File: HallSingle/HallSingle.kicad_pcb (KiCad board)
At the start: 2 copper layers, 12 x 26 mm, 10 parts, among them J1 Conn_01x03, U1 SS49E, U2 TS331ILT

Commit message: Added Voron Logo and filled missing resistor value
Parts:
- added G***: LOGO, HallEffect:VoronLogo_6pt5mm_silkScreen, B.Cu at (144.0, 61.0)
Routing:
- net Signal: track 21.4 -> 24.4 mm
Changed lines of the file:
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@@
     (thickness 1.6)
     (drawings 9)
-    (tracks 29)
+    (tracks 28)
     (zones 0)
-    (modules 10)
+    (modules 11)
     (nets 8)
   )
@@
     (add_net GND)
   )
+  (module HallEffect:VoronLogo_6pt5mm_silkScreen (layer B.Cu)
+    (at 144 61 270)
+    (fp_text reference G*** (at 0 0 270) (layer B.SilkS) hide
+      (effects (font (size 1.524 1.524) (thickness 0.3)) (justify mirror))
+    )
+    (fp_text value LOGO (at 0.75 0 270) (layer B.SilkS) hide
+      (effects (font (size 1.524 1.524) (thickness 0.3)) (justify mirror))
+    )
+    (fp_poly (pts (xy 2.7686 1.64985) (xy 2.7686 -1.649849) (xy 1.379308 -2.450524) (xy 1.039339 -2.646185)
+      (xy 0.729012 -2.824267) (xy 0.458882 -2.978754) (xy 0.239505 -3.10363) (xy 0.081439 -3.192877)
+      (xy -0.004761 -3.240478) (xy -0.017692 -3.24677) (xy -0.061819 -3.221166) (xy -0.183209 -3.150713)
+      (xy -0.371255 -3.041566) (xy -0.615351 -2.899881) (xy -0.904891 -2.731815) (xy -1.229269 -2.543525)
+      (xy -1.397 -2.446162) (xy -2.622352 -1.734876) (xy -1.566334 -1.734876) (xy -1.527559 -1.754402)
+      (xy -1.409521 -1.769187) (xy -1.234533 -1.776891) (xy -1.159934 -1.777479) (xy -0.7366 -1.776959)
+      (xy -0.722179 -1.755076) (xy 0 -1.755076) (xy 0.04685 -1.765563) (xy 0.171616 -1.7735)
+      (xy 0.350623 -1.777596) (xy 0.4191 -1.777886) (xy 0.8382 -1.777772) (xy 1.3208 -1.034043)
+      (xy 1.485838 -0.779678) (xy 1.637963 -0.545166) (xy 1.765863 -0.347951) (xy 1.858223 -0.205476)
+      (xy 1.897288 -0.145156) (xy 1.991177 0) (xy 1.129093 0) (xy 0.564546 -0.866076)
+      (xy 0.394034 -1.128735) (xy 0.244186 -1.361619) (xy 0.123286 -1.551683) (xy 0.039618 -1.685882)
+      (xy 0.001465 -1.751172) (xy 0 -1.755076) (xy -0.722179 -1.755076) (xy 0.4064 -0.042603)
+      (xy 0.654036 0.333568) (xy 0.884037 0.683745) (xy 1.09042 0.998762) (xy 1.267202 1.269449)
+      (xy 1.408399 1.486639) (xy 1.508029 1.641163) (xy 1.560108 1.723852) (xy 1.566333 1.734877)
+      (xy 1.527558 1.754403) (xy 1.40952 1.769188) (xy 1.234532 1.776892) (xy 1.159933 1.77748)
+      (xy 0.7366 1.77696) (xy -0.4064 0.042604) (xy -0.654037 -0.333567) (xy -0.884038 -0.683744)
+      (xy -1.090421 -0.998761) (xy -1.267203 -1.269448) (xy -1.4084 -1.486638) (xy -1.50803 -1.641162)
+      (xy -1.560109 -1.723851) (xy -1.566334 -1.734876) (xy -2.622352 -1.734876) (xy -2.7686 -1.649983)
+      (xy -2.7686 0) (xy -1.991178 0) (xy -1.129094 0) (xy -0.564547 0.866077)
+      (xy -0.394035 1.128736) (xy -0.244187 1.36162) (xy -0.123287 1.551684) (xy -0.039619 1.685883)
+      (xy -0.001466 1.751173) (xy 0 1.755077) (xy -0.046851 1.765564) (xy -0.171617 1.773501)
+      (xy -0.350624 1.777597) (xy -0.4191 1.777887) (xy -0.8382 1.777773) (xy -1.3208 1.034044)
+      (xy -1.485839 0.779679) (xy -1.637964 0.545167) (xy -1.765864 0.347952) (xy -1.858224 0.205477)
+      (xy -1.897289 0.145157) (xy -1.991178 0) (xy -2.7686 0) (xy -2.7686 1.64985)
+      (xy 0 3.245448) (xy 2.7686 1.64985)) (layer B.SilkS) (width 0.01))
+  )
   (module HallEffect:SOT-23-5 (layer F.Cu)
     (at 147.5535 59.563)
@@
       (effects (font (size 1 1) (thickness 0.15)))
     )
-    (fp_text value R (at 0 1.65 90) (layer F.Fab)
+    (fp_text value R (at 3.3805 -0.0635 90) (layer F.Fab)
       (effects (font (size 1 1) (thickness 0.15)))
     )
@@
       (effects (font (size 1 1) (thickness 0.15)))
     )
-    (fp_text value 10K (at 0 1.65) (layer F.Fab)
+    (fp_text value 10K (at 0.3325 1.4605) (layer F.Fab)
       (effects (font (size 1 1) (thickness 0.15)))
     )
@@
     (attr smd)
     (fp_text reference D1 (at -0.063 -1.443 90) (layer F.SilkS)
-      (effects (font (size 0.5 0.5) (thickness 0.125)))
+      (effects (font (size 0.75 0.75) (thickness 0.125)))
     )
     (fp_text value LED (at 0 1.65 90) (layer F.Fab)
@@
       (effects (font (size 1 1) (thickness 0.15)))
     )
-    (fp_text value 1uF (at 0 1.65 90) (layer F.Fab)
+    (fp_text value 1uF (at 3.8885 0.254 90) (layer F.Fab)
       (effects (font (size 1 1) (thickness 0.15)))
     )
@@
       (effects (font (size 1 1) (thickness 0.15)))
     )
-    (fp_text value 0.1uF (at 0 1.65) (layer F.Fab)
+    (fp_text value 0.1uF (at 0 -2.0955) (layer F.Fab)
       (effects (font (size 1 1) (thickness 0.15)))
     )
@@
   (segment (start 148.463 62.738) (end 146.7485 62.738) (width 0.3048) (layer F.Cu) (net 2))
   (segment (start 146.558 64.9605) (end 146.558 62.9285) (width 0.3048) (layer F.Cu) (net 2))
+  (segment (start 148.6535 75.2665) (end 148 75.92) (width 0.3048) (layer B.Cu) (net 5))
+  (segment (start 148.6535 60.5155) (end 148.6535 75.2665) (width 0.3048) (layer B.Cu) (net 5))
   (segment (start 144.526 64.643) (end 148.6535 60.5155) (width 0.3048) (layer B.Cu) (net 5))
   (segment (start 141.6685 64.643) (end 144.526 64.643) (width 0.3048) (layer B.Cu) (net 5))
-  (segment (start 147.150001 67.267001) (end 144.526 64.643) (width 0.3048) (layer B.Cu) (net 5))
-  (segment (start 147.150001 75.070001) (end 147.150001 67.267001) (width 0.3048) (layer B.Cu) (net 5))
-  (segment (start 148 75.92) (end 147.150001 75.070001) (width 0.3048) (layer B.Cu) (net 5))
   (segment (start 146.451 58.6105) (end 146.4535 58.613) (width 0.3048) (layer F.Cu) (net 7))
   (segment (start 144.272 58.6105) (end 146.451 58.6105) (width 0.3048) (layer F.Cu) (net 7))

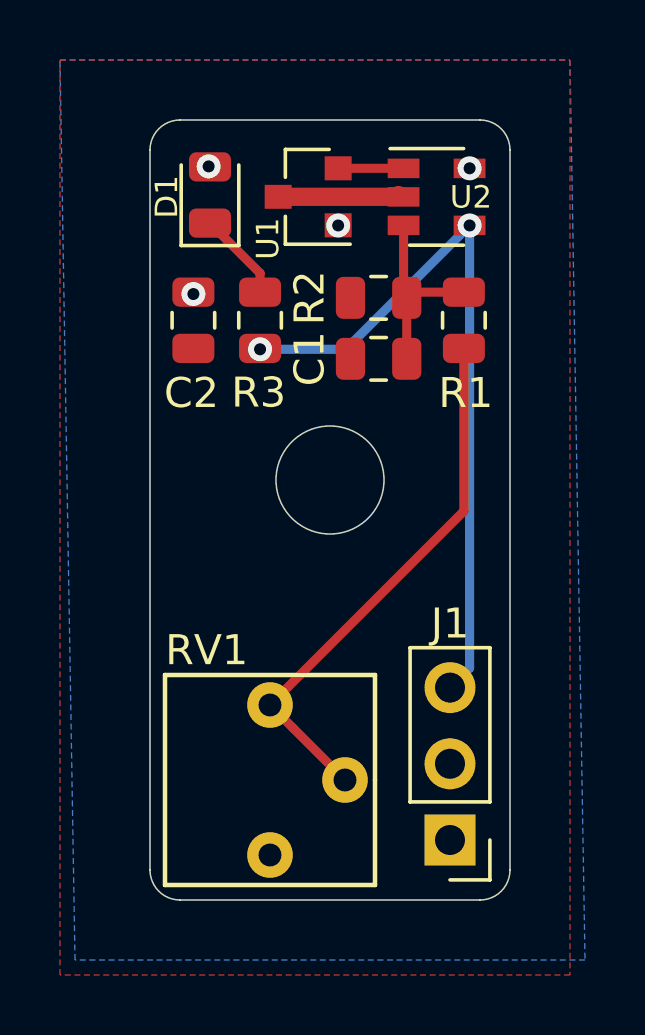
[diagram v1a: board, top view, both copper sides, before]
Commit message: Reduced total length 1mm to remove interferance with M5 in V1.8 Y mount
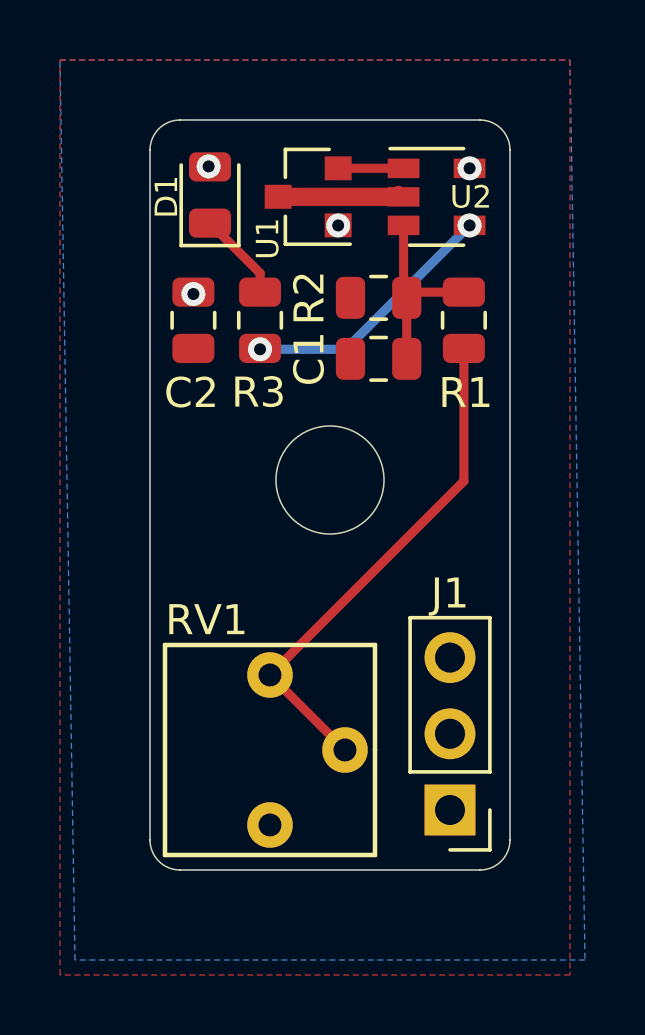
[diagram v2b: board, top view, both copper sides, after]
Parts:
- moved J1 1.00 mm to (148.0, 80.0)
- moved RV1 1.00 mm to (142.0, 78.0)
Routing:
- net Signal: track 24.4 -> 8.69 mm
- net Net-(R1-Pad1): track 18.1 -> 17.1 mm
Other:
- board size 12 x 26 mm -> 12 x 25 mm
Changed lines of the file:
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@@
     (thickness 1.6)
     (drawings 9)
-    (tracks 28)
+    (tracks 25)
     (zones 0)
     (modules 11)
@@
     (solder_mask_min_width 0.25)
     (aux_axis_origin 0 0)
-    (visible_elements FFFFFF7F)
+    (visible_elements 7FFFFFFF)
     (pcbplotparams
       (layerselection 0x010fc_ffffffff)
@@
   )
   (module HallEffect:CT6EP103 (layer F.Cu)
-    (at 142 79 270)
+    (at 142 78 270)
     (fp_text reference RV1 (at -4.324 2.1095 180) (layer F.SilkS)
       (effects (font (size 1 1) (thickness 0.15)))
@@
   )
   (module HallEffect:PinHeader_1x03_P2.54mm_Vertical (layer F.Cu)
-    (at 148 81 180)
+    (at 148 80 180)
     (descr "Through hole straight pin header, 1x03, 2.54mm pitch, single row")
     (tags "Through hole pin header THT 1x03 2.54mm single row")
@@
     )
   )
-  (gr_arc (start 139 82) (end 138 82) (angle -90) (layer Edge.Cuts) (width 0.05))
-  (gr_arc (start 149 82) (end 149 83) (angle -90) (layer Edge.Cuts) (width 0.05))
+  (gr_arc (start 139 81) (end 138 81) (angle -90) (layer Edge.Cuts) (width 0.05))
+  (gr_arc (start 149 81) (end 149 82) (angle -90) (layer Edge.Cuts) (width 0.05))
   (gr_arc (start 149 58) (end 150 58) (angle -90) (layer Edge.Cuts) (width 0.05))
   (gr_arc (start 139 58) (end 139 57) (angle -90) (layer Edge.Cuts) (width 0.05))
-  (gr_line (start 138 58) (end 138 82) (layer Edge.Cuts) (width 0.05))
-  (gr_line (start 149 83) (end 139 83) (layer Edge.Cuts) (width 0.05))
+  (gr_line (start 138 58) (end 138 81) (layer Edge.Cuts) (width 0.05))
+  (gr_line (start 149 82) (end 139 82) (layer Edge.Cuts) (width 0.05))
   (gr_circle (center 144 69) (end 145.8 69) (layer Edge.Cuts) (width 0.05))
-  (gr_line (start 150 58) (end 150 82) (layer Edge.Cuts) (width 0.05))
+  (gr_line (start 150 58) (end 150 81) (layer Edge.Cuts) (width 0.05))
   (gr_line (start 139 57) (end 149 57) (layer Edge.Cuts) (width 0.05))
-  (via (at 148.6535 58.6105) (size 0.8) (drill 0.4) (layers F.Cu B.Cu) (net 3))
-  (via (at 139.446 62.8015) (size 0.8) (drill 0.4) (layers F.Cu B.Cu) (net 3))
   (segment (start 146.284 59.5) (end 146.347 59.563) (width 0.6096) (layer F.Cu) (net 1))
   (segment (start 146.451 59.5605) (end 146.4535 59.563) (width 0.6096) (layer F.Cu) (net 1))
   (segment (start 142.272 59.5605) (end 146.451 59.5605) (width 0.6096) (layer F.Cu) (net 1))
-  (via (at 148.6535 60.5155) (size 0.8) (drill 0.4) (layers F.Cu B.Cu) (net 5))
-  (via (at 139.954 58.547) (size 0.8) (drill 0.4) (layers F.Cu B.Cu) (net 3))
-  (via (at 144.272 60.5155) (size 0.8) (drill 0.4) (layers F.Cu B.Cu) (net 3))
   (segment (start 148.45 62.725) (end 148.463 62.738) (width 0.3048) (layer F.Cu) (net 2))
   (segment (start 147.9885 62.738) (end 148.463 62.738) (width 0.3048) (layer F.Cu) (net 2))
-  (segment (start 141.6685 62.106) (end 140 60.4375) (width 0.3048) (layer F.Cu) (net 4))
-  (segment (start 141.6685 62.738) (end 141.6685 62.106) (width 0.3048) (layer F.Cu) (net 4))
-  (via (at 141.6685 64.643) (size 0.8) (drill 0.4) (layers F.Cu B.Cu) (net 5))
-  (segment (start 142.761999 77.261999) (end 144.5 79) (width 0.3048) (layer F.Cu) (net 6))
-  (segment (start 142 76.5) (end 142.761999 77.261999) (width 0.3048) (layer F.Cu) (net 6))
-  (segment (start 148.463 70.037) (end 148.463 64.613) (width 0.3048) (layer F.Cu) (net 6))
-  (segment (start 142 76.5) (end 148.463 70.037) (width 0.3048) (layer F.Cu) (net 6))
   (segment (start 146.4535 62.824) (end 146.558 62.9285) (width 0.3048) (layer F.Cu) (net 2))
   (segment (start 146.4535 60.513) (end 146.4535 62.824) (width 0.3048) (layer F.Cu) (net 2))
@@
   (segment (start 148.463 62.738) (end 146.7485 62.738) (width 0.3048) (layer F.Cu) (net 2))
   (segment (start 146.558 64.9605) (end 146.558 62.9285) (width 0.3048) (layer F.Cu) (net 2))
-  (segment (start 148.6535 75.2665) (end 148 75.92) (width 0.3048) (layer B.Cu) (net 5))
-  (segment (start 148.6535 60.5155) (end 148.6535 75.2665) (width 0.3048) (layer B.Cu) (net 5))
+  (via (at 148.6535 58.6105) (size 0.8) (drill 0.4) (layers F.Cu B.Cu) (net 3))
+  (via (at 139.446 62.8015) (size 0.8) (drill 0.4) (layers F.Cu B.Cu) (net 3))
+  (via (at 139.954 58.547) (size 0.8) (drill 0.4) (layers F.Cu B.Cu) (net 3))
+  (via (at 144.272 60.5155) (size 0.8) (drill 0.4) (layers F.Cu B.Cu) (net 3))
+  (segment (start 141.6685 62.106) (end 140 60.4375) (width 0.3048) (layer F.Cu) (net 4))
+  (segment (start 141.6685 62.738) (end 141.6685 62.106) (width 0.3048) (layer F.Cu) (net 4))
+  (via (at 148.6535 60.5155) (size 0.8) (drill 0.4) (layers F.Cu B.Cu) (net 5))
+  (via (at 141.6685 64.643) (size 0.8) (drill 0.4) (layers F.Cu B.Cu) (net 5))
   (segment (start 144.526 64.643) (end 148.6535 60.5155) (width 0.3048) (layer B.Cu) (net 5))
   (segment (start 141.6685 64.643) (end 144.526 64.643) (width 0.3048) (layer B.Cu) (net 5))
+  (segment (start 144.5 78) (end 142 75.5) (width 0.3048) (layer F.Cu) (net 6))
+  (segment (start 148.463 69.037) (end 148.463 64.613) (width 0.3048) (layer F.Cu) (net 6))
+  (segment (start 142 75.5) (end 148.463 69.037) (width 0.3048) (layer F.Cu) (net 6))
   (segment (start 146.451 58.6105) (end 146.4535 58.613) (width 0.3048) (layer F.Cu) (net 7))
   (segment (start 144.272 58.6105) (end 146.451 58.6105) (width 0.3048) (layer F.Cu) (net 7))

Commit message: fixed missed trace
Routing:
- net Signal: track 8.69 -> 23.7 mm
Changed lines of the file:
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@@
     (thickness 1.6)
     (drawings 9)
-    (tracks 25)
+    (tracks 29)
     (zones 0)
     (modules 11)
@@
   (segment (start 144.526 64.643) (end 148.6535 60.5155) (width 0.3048) (layer B.Cu) (net 5))
   (segment (start 141.6685 64.643) (end 144.526 64.643) (width 0.3048) (layer B.Cu) (net 5))
+  (segment (start 148.849999 74.070001) (end 148 74.92) (width 0.3048) (layer B.Cu) (net 5))
+  (segment (start 149.053499 60.915499) (end 149.053499 73.866501) (width 0.3048) (layer B.Cu) (net 5))
+  (segment (start 149.053499 73.866501) (end 148.849999 74.070001) (width 0.3048) (layer B.Cu) (net 5))
+  (segment (start 148.6535 60.5155) (end 149.053499 60.915499) (width 0.3048) (layer B.Cu) (net 5))
   (segment (start 144.5 78) (end 142 75.5) (width 0.3048) (layer F.Cu) (net 6))
   (segment (start 148.463 69.037) (end 148.463 64.613) (width 0.3048) (layer F.Cu) (net 6))

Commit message: Reduced size due to almost certain interferance from screw heads on v1.8 Y.
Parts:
- R3: value R -> 1k
- moved RV1 1.50 mm to (142.0, 76.5)
- moved J1 1.42 mm to (148.0, 78.6)
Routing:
- net Signal: track 23.7 -> 22.3 mm
- net Net-(R1-Pad1): track 17.1 -> 16.2 mm
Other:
- board size 12 x 25 mm -> 12 x 24 mm
- board text added: "+5v"
- board text added: "G"
- board text added: "S"
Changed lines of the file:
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@@
   (general
     (thickness 1.6)
-    (drawings 9)
-    (tracks 29)
+    (drawings 12)
+    (tracks 31)
     (zones 0)
     (modules 11)
@@
   )
   (module HallEffect:CT6EP103 (layer F.Cu)
-    (at 142 78 270)
+    (at 142 76.5 270)
     (fp_text reference RV1 (at -4.324 2.1095 180) (layer F.SilkS)
       (effects (font (size 1 1) (thickness 0.15)))
@@
       (effects (font (size 1 1) (thickness 0.15)))
     )
-    (fp_text value R (at 3.3805 -0.0635 90) (layer F.Fab)
+    (fp_text value 1k (at 3.3805 -0.0635 90) (layer F.Fab)
       (effects (font (size 1 1) (thickness 0.15)))
     )
@@
   )
   (module HallEffect:PinHeader_1x03_P2.54mm_Vertical (layer F.Cu)
-    (at 148 80 180)
+    (at 148 78.58 180)
     (descr "Through hole straight pin header, 1x03, 2.54mm pitch, single row")
     (tags "Through hole pin header THT 1x03 2.54mm single row")
@@
     )
   )
-  (gr_arc (start 139 81) (end 138 81) (angle -90) (layer Edge.Cuts) (width 0.05))
-  (gr_arc (start 149 81) (end 149 82) (angle -90) (layer Edge.Cuts) (width 0.05))
+  (gr_text G (at 146.304 76.2) (layer B.SilkS)
+    (effects (font (size 1 1) (thickness 0.15)) (justify mirror))
+  )
+  (gr_text +5v (at 145.542 78.486) (layer B.SilkS)
+    (effects (font (size 1 1) (thickness 0.15)) (justify mirror))
+  )
+  (gr_text S (at 146.304 73.5) (layer B.SilkS)
+    (effects (font (size 1 1) (thickness 0.15)) (justify mirror))
+  )
+  (gr_arc (start 139 80) (end 138 80) (angle -90) (layer Edge.Cuts) (width 0.05))
+  (gr_arc (start 149 80) (end 149 81) (angle -90) (layer Edge.Cuts) (width 0.05))
   (gr_arc (start 149 58) (end 150 58) (angle -90) (layer Edge.Cuts) (width 0.05))
   (gr_arc (start 139 58) (end 139 57) (angle -90) (layer Edge.Cuts) (width 0.05))
-  (gr_line (start 138 58) (end 138 81) (layer Edge.Cuts) (width 0.05))
-  (gr_line (start 149 82) (end 139 82) (layer Edge.Cuts) (width 0.05))
+  (gr_line (start 138 58) (end 138 80) (layer Edge.Cuts) (width 0.05))
+  (gr_line (start 149 81) (end 139 81) (layer Edge.Cuts) (width 0.05))
   (gr_circle (center 144 69) (end 145.8 69) (layer Edge.Cuts) (width 0.05))
-  (gr_line (start 150 58) (end 150 81) (layer Edge.Cuts) (width 0.05))
+  (gr_line (start 150 58) (end 150 80) (layer Edge.Cuts) (width 0.05))
   (gr_line (start 139 57) (end 149 57) (layer Edge.Cuts) (width 0.05))
   (segment (start 146.284 59.5) (end 146.347 59.563) (width 0.6096) (layer F.Cu) (net 1))
@@
   (via (at 139.954 58.547) (size 0.8) (drill 0.4) (layers F.Cu B.Cu) (net 3))
   (via (at 144.272 60.5155) (size 0.8) (drill 0.4) (layers F.Cu B.Cu) (net 3))
+  (segment (start 143.07763 74) (end 142 74) (width 0.3048) (layer F.Cu) (net 6))
   (segment (start 141.6685 62.106) (end 140 60.4375) (width 0.3048) (layer F.Cu) (net 4))
   (segment (start 141.6685 62.738) (end 141.6685 62.106) (width 0.3048) (layer F.Cu) (net 4))
@@
   (segment (start 144.526 64.643) (end 148.6535 60.5155) (width 0.3048) (layer B.Cu) (net 5))
   (segment (start 141.6685 64.643) (end 144.526 64.643) (width 0.3048) (layer B.Cu) (net 5))
-  (segment (start 148.849999 74.070001) (end 148 74.92) (width 0.3048) (layer B.Cu) (net 5))
-  (segment (start 149.053499 60.915499) (end 149.053499 73.866501) (width 0.3048) (layer B.Cu) (net 5))
-  (segment (start 149.053499 73.866501) (end 148.849999 74.070001) (width 0.3048) (layer B.Cu) (net 5))
+  (segment (start 148.849999 72.650001) (end 148 73.5) (width 0.3048) (layer B.Cu) (net 5))
+  (segment (start 149.053499 60.915499) (end 149.053499 72.446501) (width 0.3048) (layer B.Cu) (net 5))
+  (segment (start 149.053499 72.446501) (end 148.849999 72.650001) (width 0.3048) (layer B.Cu) (net 5))
   (segment (start 148.6535 60.5155) (end 149.053499 60.915499) (width 0.3048) (layer B.Cu) (net 5))
-  (segment (start 144.5 78) (end 142 75.5) (width 0.3048) (layer F.Cu) (net 6))
-  (segment (start 148.463 69.037) (end 148.463 64.613) (width 0.3048) (layer F.Cu) (net 6))
-  (segment (start 142 75.5) (end 148.463 69.037) (width 0.3048) (layer F.Cu) (net 6))
+  (segment (start 148.463 64.613) (end 146.794399 66.281601) (width 0.3048) (layer F.Cu) (net 6))
+  (segment (start 146.794399 66.281601) (end 146.794399 70.283231) (width 0.3048) (layer F.Cu) (net 6))
+  (segment (start 146.794399 70.283231) (end 143.07763 74) (width 0.3048) (layer F.Cu) (net 6))
+  (segment (start 144.5 76.5) (end 142 74) (width 0.3048) (layer F.Cu) (net 6))
   (segment (start 146.451 58.6105) (end 146.4535 58.613) (width 0.3048) (layer F.Cu) (net 7))
   (segment (start 144.272 58.6105) (end 146.451 58.6105) (width 0.3048) (layer F.Cu) (net 7))
